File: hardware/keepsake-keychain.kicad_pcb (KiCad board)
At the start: 2 copper layers, 80 x 30 mm, 95 parts, among them Q1 MMFTP4042K, Q2 MMFTP4042K, Q3 MMFTP4042K, Q4 MMFTP4042K, SW1 SPDT Power Switch, SW2 PTS636 SK25J SMTR LFS, U1 74HC595, U2 74HC595, U3 74HC595, U4 Op Amp, U5 ATTINY1614, U6 MEMS Microphone

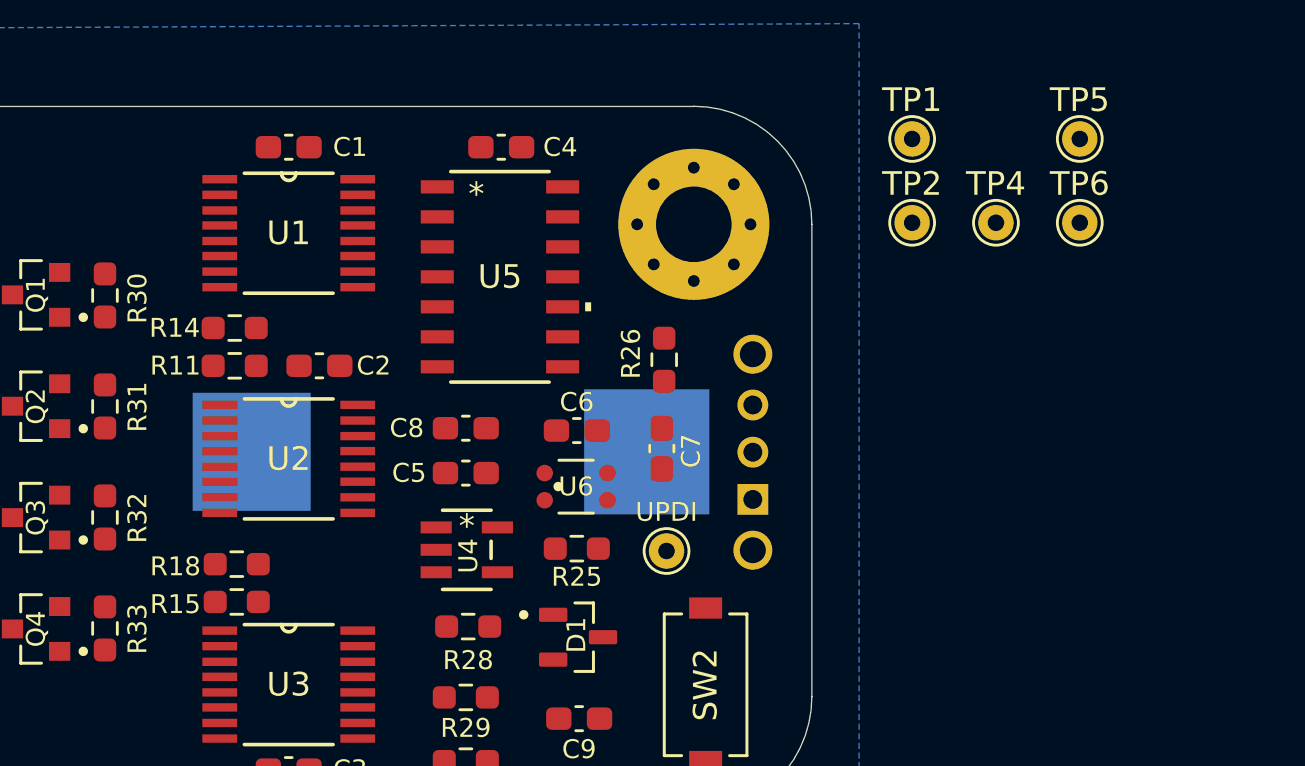
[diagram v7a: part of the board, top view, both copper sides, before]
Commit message: Fix errors from unassigned pins
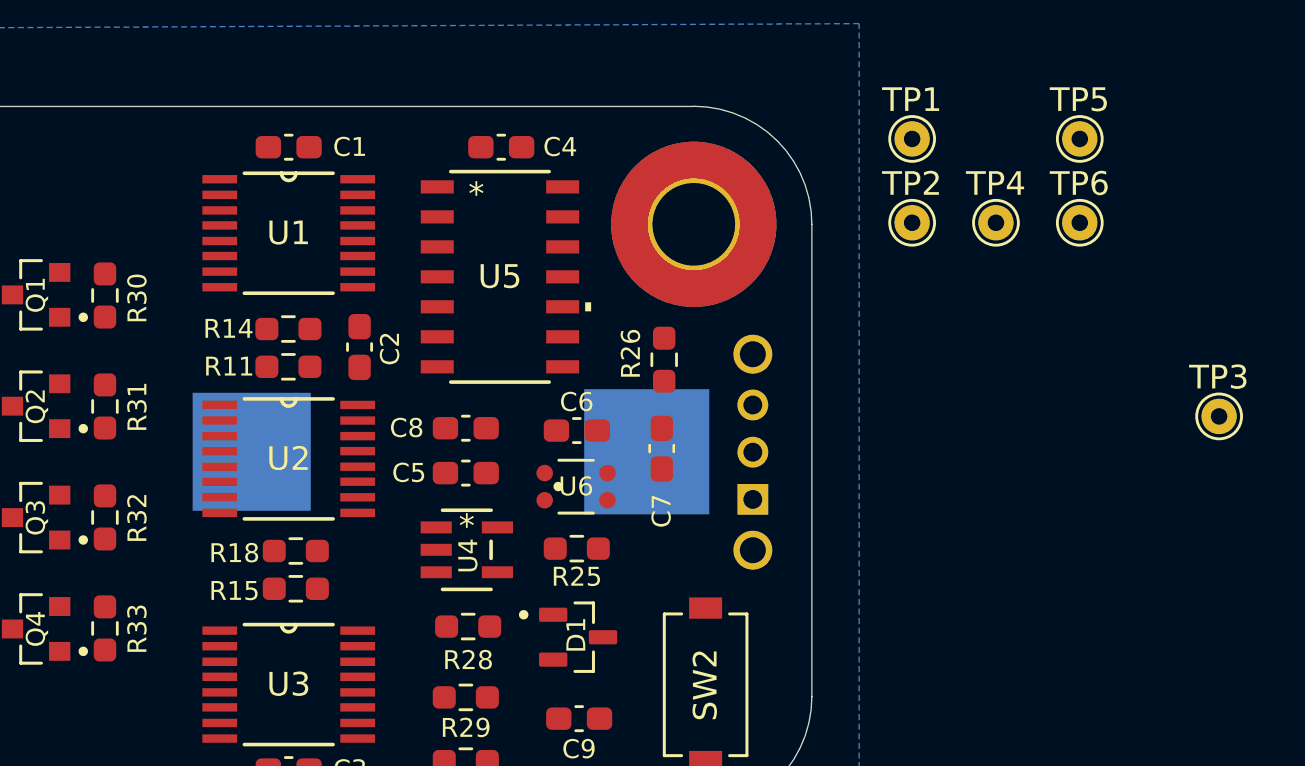
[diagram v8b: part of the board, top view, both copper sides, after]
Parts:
- removed UPDI: 5002, TestPoint:TestPoint_THTPad_D1.5mm_Drill0.7mm
- added TP3: 5002, TestPoint:TestPoint_THTPad_D1.5mm_Drill0.7mm, F.Cu at (207.1, 92.6)
- H1: footprint MountingHole:MountingHole_3.2mm_M3_Pad_Via -> MountingHole:MountingHole_3.5mm_Pad_TopBottom
- moved R15 2.56 mm to (168.0, 99.9)
- moved R18 2.56 mm to (168.0, 98.3)
- moved R11 2.28 mm to (167.7, 90.5)
- moved R14 2.28 mm to (167.7, 88.9)
- moved C2 1.88 mm to (170.7, 89.6), turned to 90 degrees
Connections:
- H1 pad 1: (no net) -> unconnected-(H1-Pad1)_2
- SW1 pad SH1: (no net) -> unconnected-(SW1-PadSH1)
- SW1 pad SH2: (no net) -> unconnected-(SW1-PadSH2)
